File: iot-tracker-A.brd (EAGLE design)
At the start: 23.5 x 20 mm, 24 parts, among them U1 ESP-WROOM-02, U2 TPL5111DDCR

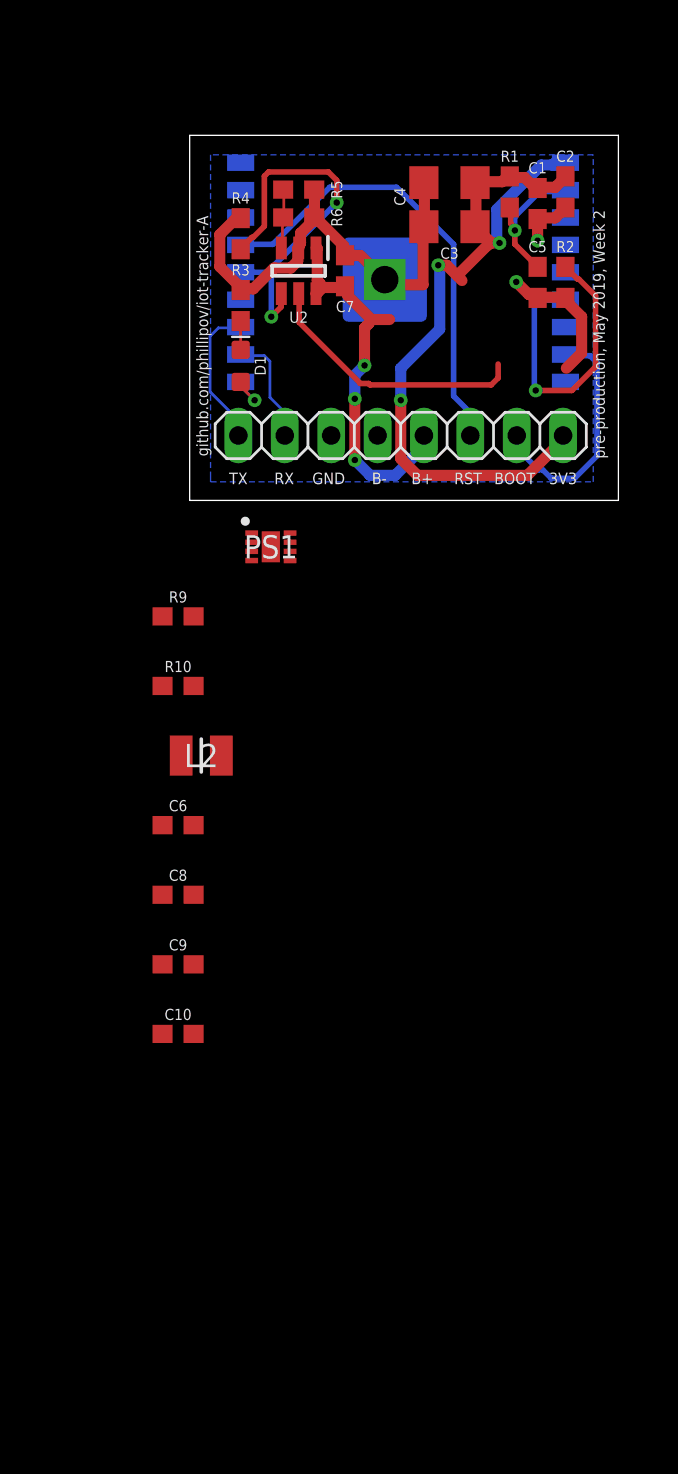
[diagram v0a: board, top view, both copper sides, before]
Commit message: Changed bulk capacitors to tantalum; minor component edits
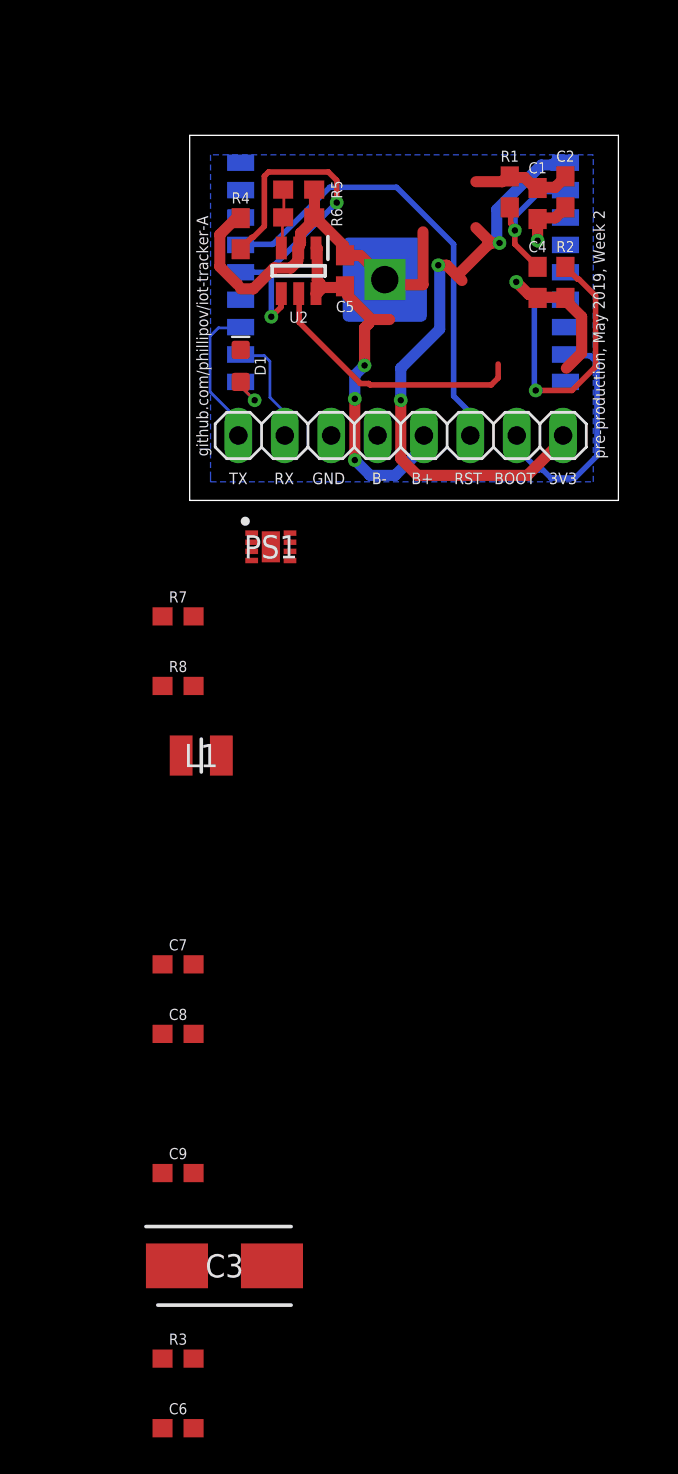
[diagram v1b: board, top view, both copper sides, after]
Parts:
- removed C10: 10uF, SparkFun-Capacitors:0603
- C3: value 100uF -> 220uF; device SparkFun-Capacitors:1206 -> IOT-Tracker-A:CAPPM7343X430N
- C4: value 100uF -> 0.1uF; device SparkFun-Capacitors:1206 -> SparkFun-Capacitors:0603
- C6, C7: value 0.1uF -> 10uF
- C8: value 100pF -> 10uF
- C9: value 10uF -> 10pF
- R3: value 100 -> 1k
- moved C3 58.2 mm to (2.54, -41.9)
- moved R3 57.8 mm to (0.00, -47.0), turned to 0 degrees
- moved C7 39.1 mm to (0.00, -25.4), turned to 0 degrees
- moved C6 33.0 mm to (0.00, -50.8)
- moved C9 11.4 mm to (0.00, -36.8)
- moved C5 10.6 mm to (9.14, 12.6), turned to 270 degrees
- moved C8 7.62 mm to (0.00, -29.2)
- moved C4 7.29 mm to (19.7, 11.9), turned to 90 degrees
- renumbered L2 to L1, R10 to R8, R9 to R7
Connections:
- net 3.3V: now also C3.1, C7.1, C8.1, C9.2; no longer C10.1, C3.2, C4.2, C8.2, C9.1
- net EN: now also C4.2; no longer C5.2
- net GND: now also C3.2, C6.2, C7.2, C8.2; no longer C10.2, C3.1, C6.1, C7.1, C9.2
- net N$1: now also C9.1; no longer C8.1
- net V_BATT: now also C5.2, C6.1; no longer C6.2, C7.2
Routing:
- net GND: track 37.0 -> 33.9 mm
- net 3.3V: track 42.5 -> 39.9 mm
- net LED_GND: track 1.57 -> 0.00 mm

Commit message: Started basic board layout
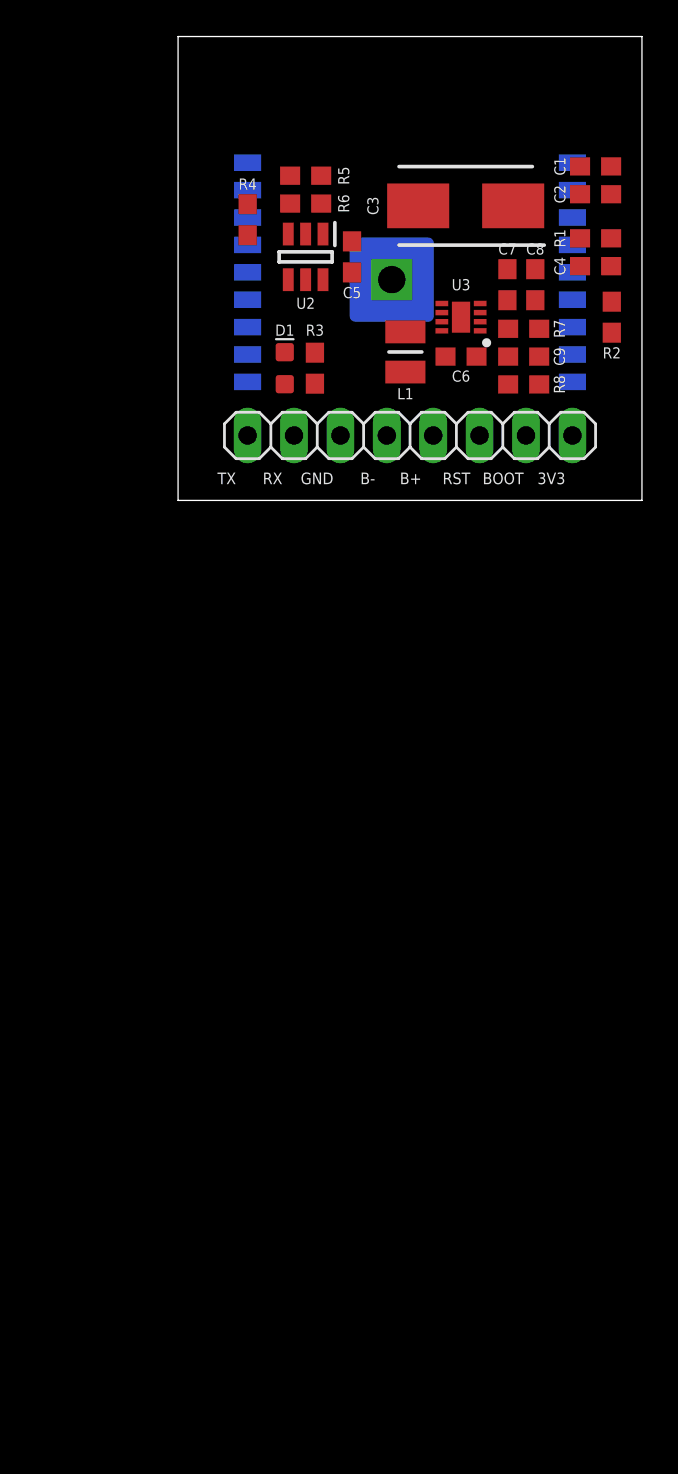
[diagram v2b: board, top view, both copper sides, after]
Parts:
- removed PS1: TPS61021ADSGR, IOT-Tracker-A:SON50P200X200X80-9N
- added U3: TPS61021ADSGR, IOT-Tracker-A:SON50P200X200X80-9N
- moved C6 60.7 mm to (15.5, 7.87)
- moved C3 59.5 mm to (15.7, 16.1), turned to 180 degrees
- moved R3 54.7 mm to (7.49, 7.24), turned to 270 degrees
- moved C9 48.5 mm to (18.9, 7.87)
- moved C8 45.4 mm to (19.6, 11.8), turned to 90 degrees
- moved C7 41.4 mm to (18.0, 11.8), turned to 90 degrees
- moved R8 25.1 mm to (18.9, 6.35)
- moved L1 24.8 mm to (12.4, 8.13), turned to 270 degrees
- moved R7 24.6 mm to (18.9, 9.40), turned to 180 degrees
- moved R1 5.34 mm to (22.9, 14.4), turned to 0 degrees
- moved C1 3.77 mm to (22.9, 18.3), turned to 180 degrees
- moved C4 3.30 mm to (22.9, 12.8), turned to 0 degrees
- moved R2 3.18 mm to (23.7, 10.0)
- moved D1 2.42 mm to (5.84, 7.24)
- moved C2 1.66 mm to (22.9, 16.8), turned to 180 degrees
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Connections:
- removed net N$1: C9.1, PS1.2, R7.2, R8.1
- new net FB: C9.1, R7.2, R8.1, U3.2
- net 3.3V: now also U3.3, U3.4; no longer PS1.3, PS1.4
- net DRVN: now also U3.5; no longer PS1.5
- net GND: now also U3.1, U3.9; no longer PS1.1, PS1.9
- net SW: now also U3.6, U3.7; no longer PS1.6, PS1.7
- net V_BATT: now also U3.8; no longer PS1.8
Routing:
- net 3.3V: track 39.9 -> 0.00 mm, vias 3 -> 0
- net GND: track 33.9 -> 0.00 mm, vias 2 -> 0
- net RST: track 25.1 -> 0.00 mm
- net V_BATT: track 21.3 -> 0.00 mm, vias 3 -> 0
- net DONE: track 21.0 -> 0.00 mm, vias 2 -> 0
- net IO15: track 16.5 -> 0.00 mm, vias 1 -> 0
- net DRVN: track 14.8 -> 0.00 mm
- net BOOT: track 13.3 -> 0.00 mm
- net EN: track 8.10 -> 0.00 mm, vias 1 -> 0
- net TX: track 7.95 -> 0.00 mm
- net RX: track 6.20 -> 0.00 mm
- net DELAY: track 3.28 -> 0.00 mm
- net IO4_LED: track 2.64 -> 0.00 mm, vias 1 -> 0
- removed copper zone on layer 16, net GND
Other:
- board size 23.5 x 20 mm -> 25.4 x 25.4 mm
- board text removed: "github.com/phillipov/iot-tracker-A"
- board text removed: "pre-production, May 2019, Week 2"

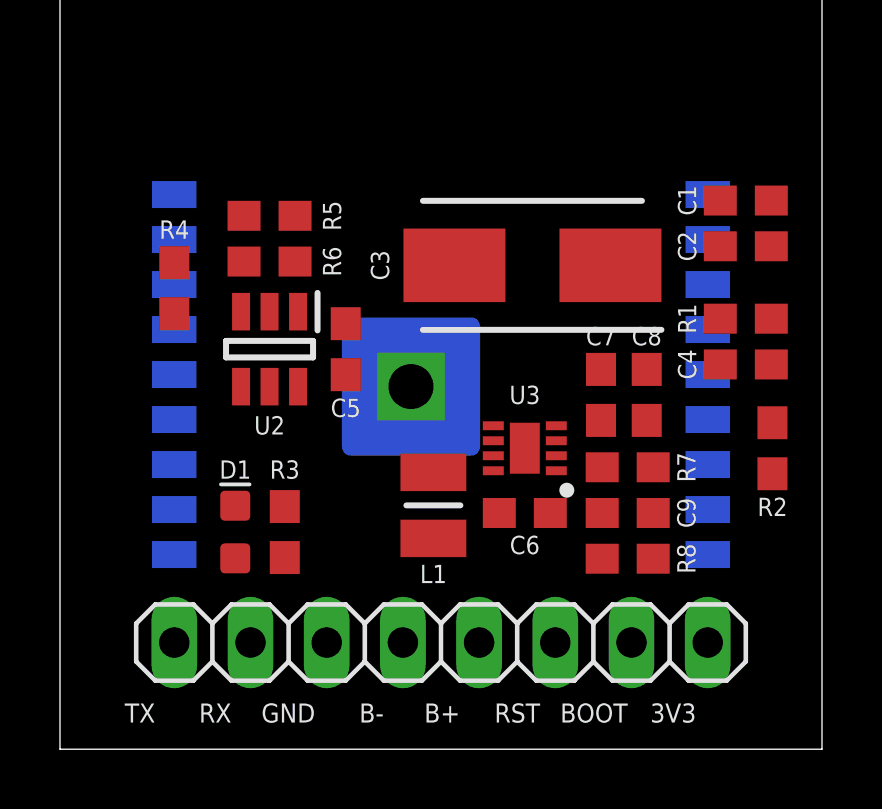
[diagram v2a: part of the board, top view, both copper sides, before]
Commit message: Slightly improved board layout
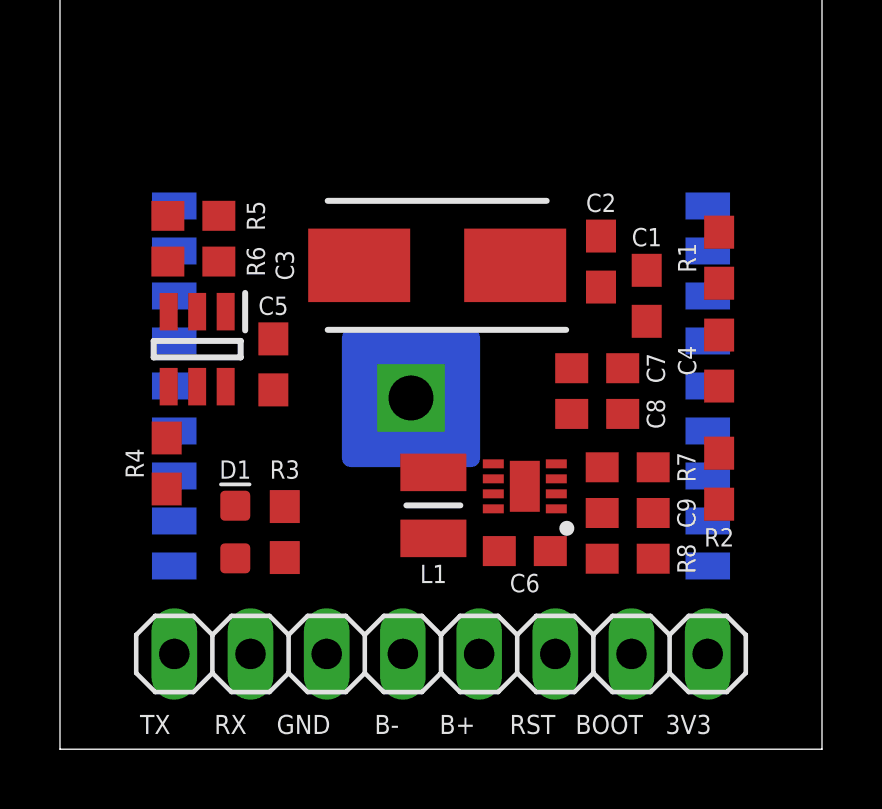
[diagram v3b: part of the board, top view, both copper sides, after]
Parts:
- moved R4 5.85 mm to (3.56, 9.53), turned to 270 degrees
- moved C2 4.85 mm to (18.0, 16.3), turned to 90 degrees
- moved C1 4.58 mm to (19.6, 15.1), turned to 90 degrees
- moved C3 3.17 mm to (12.6, 16.1)
- moved R5 2.54 mm to (4.45, 17.8)
- moved R6 2.54 mm to (4.45, 16.3)
- moved C5 2.47 mm to (7.11, 12.8)
- moved U2 2.41 mm to (4.57, 13.3)
- moved R1 2.22 mm to (22.0, 16.4), turned to 270 degrees
- moved R2 2.05 mm to (22.0, 9.02)
- moved C8 1.77 mm to (17.9, 11.2), turned to 0 degrees
- moved C6 1.27 mm to (15.5, 6.60)
- moved U3 1.27 mm to (15.5, 8.76)
- moved C4 0.90 mm to (22.0, 13.0), turned to 90 degrees
- moved C7 0.90 mm to (17.9, 12.7), turned to 0 degrees
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
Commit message: Partially routed boosting circuitry
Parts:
- moved C7 3.64 mm to (14.6, 11.2), turned to 180 degrees
- moved C8 3.64 mm to (14.6, 12.7), turned to 180 degrees
- moved R8 2.40 mm to (20.2, 8.38), turned to 90 degrees
- moved C9 1.85 mm to (17.1, 8.38), turned to 90 degrees
- moved L1 1.09 mm to (11.6, 7.49)
- moved R7 1.05 mm to (18.7, 8.38), turned to 270 degrees
- moved U3 0.97 mm to (14.6, 9.14)
- moved C6 0.92 mm to (14.6, 6.86)
- moved C1 0.63 mm to (19.6, 15.7)
- moved C5 0.63 mm to (7.11, 12.2)
- moved R2 0.63 mm to (22.0, 9.65)
- moved C2 0.51 mm to (18.0, 15.7)
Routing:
- net 3.3V: track 0.00 -> 15.7 mm, vias 0 -> 1
- net EN: track 0.00 -> 7.56 mm, vias 0 -> 1
- net FB: track 0.00 -> 5.22 mm
- net V_BATT: track 0.00 -> 3.16 mm
- net IO15: track 0.00 -> 3.12 mm, vias 0 -> 1
- net SW: track 0.00 -> 1.36 mm

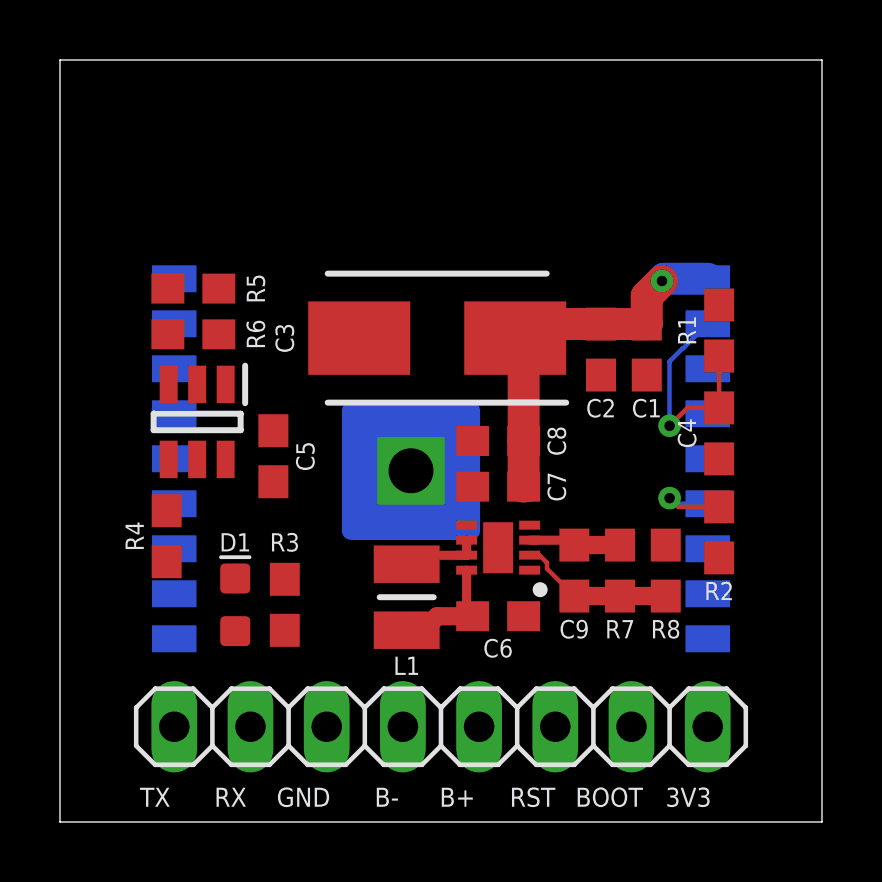
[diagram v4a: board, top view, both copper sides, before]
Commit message: Routed everything but GND
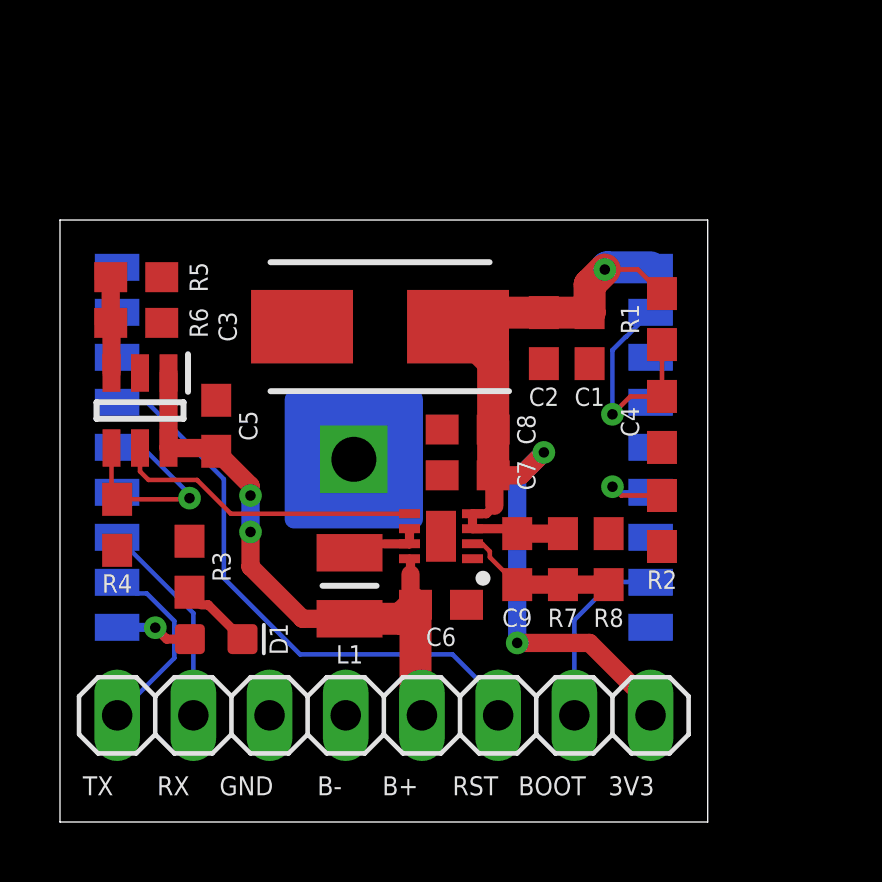
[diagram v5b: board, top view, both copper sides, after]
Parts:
- moved R3 3.42 mm to (4.32, 8.51)
- moved C5 2.16 mm to (5.21, 13.2)
- moved C1 1.94 mm to (17.7, 16.1)
- moved C3 1.94 mm to (10.7, 16.5)
- moved C4 1.94 mm to (20.1, 13.3)
- moved C6 1.94 mm to (12.7, 7.24)
- moved R1 1.94 mm to (20.1, 16.8)
- moved R2 1.94 mm to (20.1, 10.0)
- moved R7 1.94 mm to (16.8, 8.76)
- moved R8 1.94 mm to (18.3, 8.76)
- moved U3 1.94 mm to (12.7, 9.53)
- moved L1 1.94 mm to (9.65, 7.87)
- moved R5 1.94 mm to (2.54, 18.2)
- moved R6 1.94 mm to (2.54, 16.6)
- moved U2 1.94 mm to (2.67, 13.7)
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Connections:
- net RX: now also JP1.8; no longer JP1.7
- net TX: now also JP1.7; no longer JP1.8
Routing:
- net 3.3V: track 15.7 -> 35.6 mm, vias 1 -> 3
- net RST: track 0.00 -> 19.3 mm
- net V_BATT: track 3.16 -> 20.5 mm, vias 0 -> 2
- net DRVN: track 0.00 -> 10.3 mm
- net DONE: track 0.00 -> 7.41 mm, vias 0 -> 1
- net TX: track 0.00 -> 7.00 mm
- net BOOT: track 0.00 -> 6.25 mm
- net RX: track 0.00 -> 5.58 mm
- net DELAY: track 0.00 -> 3.21 mm
- net IO4_LED: track 0.00 -> 2.59 mm, vias 0 -> 1
- net LED_GND: track 0.00 -> 1.86 mm
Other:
- board size 25.4 x 25.4 mm -> 21.6 x 20.1 mm

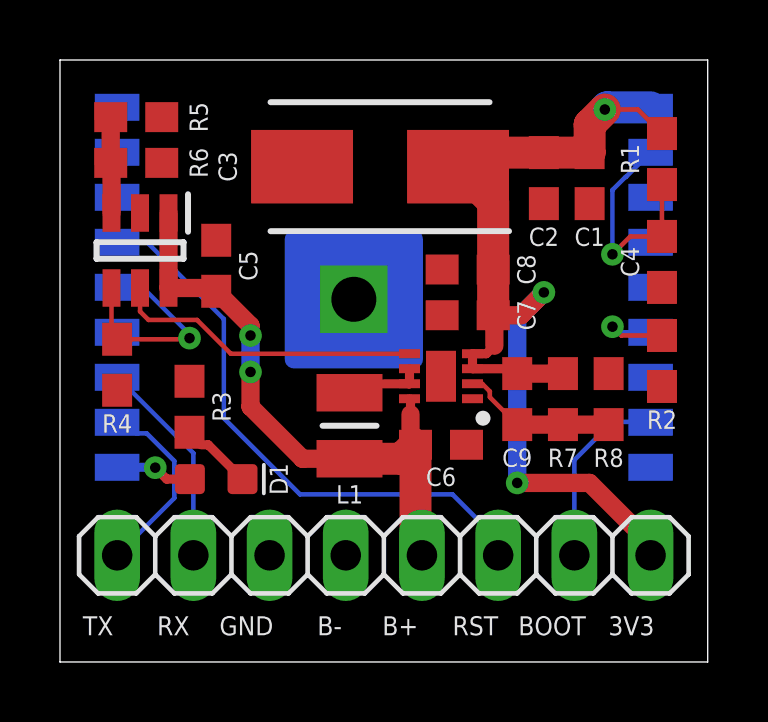
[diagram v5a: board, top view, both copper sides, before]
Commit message: Finished routing and cleared DRC
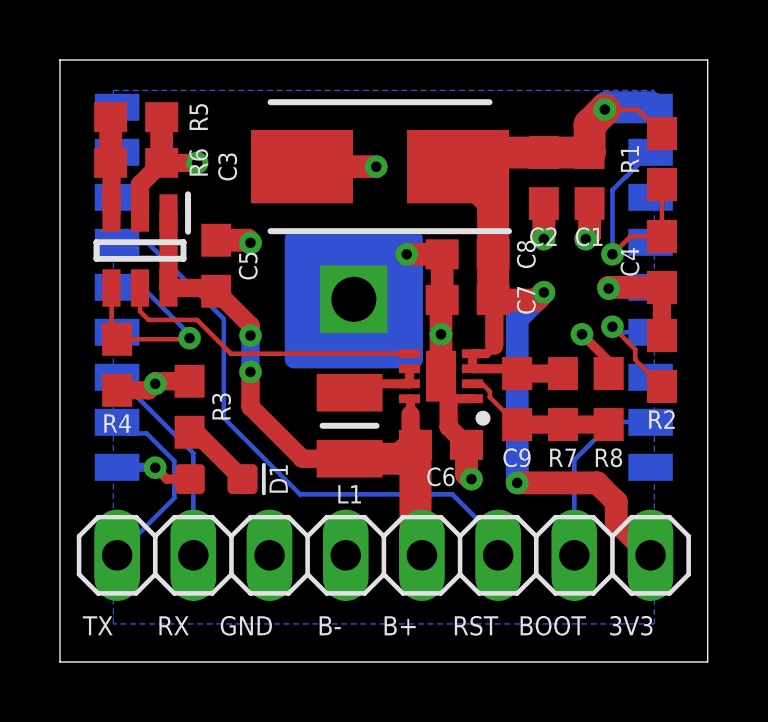
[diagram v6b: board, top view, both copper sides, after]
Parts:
- moved C8 0.51 mm to (13.6, 13.6)
- moved C7 0.51 mm to (13.6, 12.1)
- turned R2 to 90 degrees
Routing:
- net GND: track 0.00 -> 28.0 mm, vias 0 -> 11
- net SW: track 1.36 -> 2.62 mm
- net IO15: track 3.12 -> 4.03 mm
- net RX: track 5.58 -> 6.37 mm
- net LED_GND: track 1.86 -> 2.41 mm
- added copper zone on layer 16, net GND

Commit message: Board is ready for fabrication
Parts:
- moved C3 0.51 mm to (10.7, 16.0)
- moved R5 0.51 mm to (2.54, 17.7)
- moved C1 0.51 mm to (17.7, 15.6)
- moved C2 0.51 mm to (16.1, 15.6)
- moved C4 0.51 mm to (20.1, 12.8)
- moved C5 0.51 mm to (5.21, 12.7)
- moved C8 0.51 mm to (13.6, 13.1)
- moved R3 0.51 mm to (4.32, 8.00)
- moved R4 0.51 mm to (1.91, 9.40)
- moved U1 0.51 mm to (10.8, 13.1)
- moved U3 0.51 mm to (12.7, 9.02)
- moved C6 0.51 mm to (12.7, 6.73)
- moved D1 0.51 mm to (5.21, 5.59)
- moved JP1 0.51 mm to (10.8, 3.05)
- moved L1 0.51 mm to (9.65, 7.37)
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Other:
- board size 21.6 x 20.1 mm -> 21.6 x 19.6 mm
- board text added: "github.com/phillipov/iot-tracker-a"
